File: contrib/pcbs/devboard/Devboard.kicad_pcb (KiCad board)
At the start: 2 copper layers, 42.5 x 36.8 mm, 11 parts, among them J1 Power, J2 Left, J3 ARM-JTAG, J4 Right, J5 JTAG, SW1 RESET, U1 TRADFRI

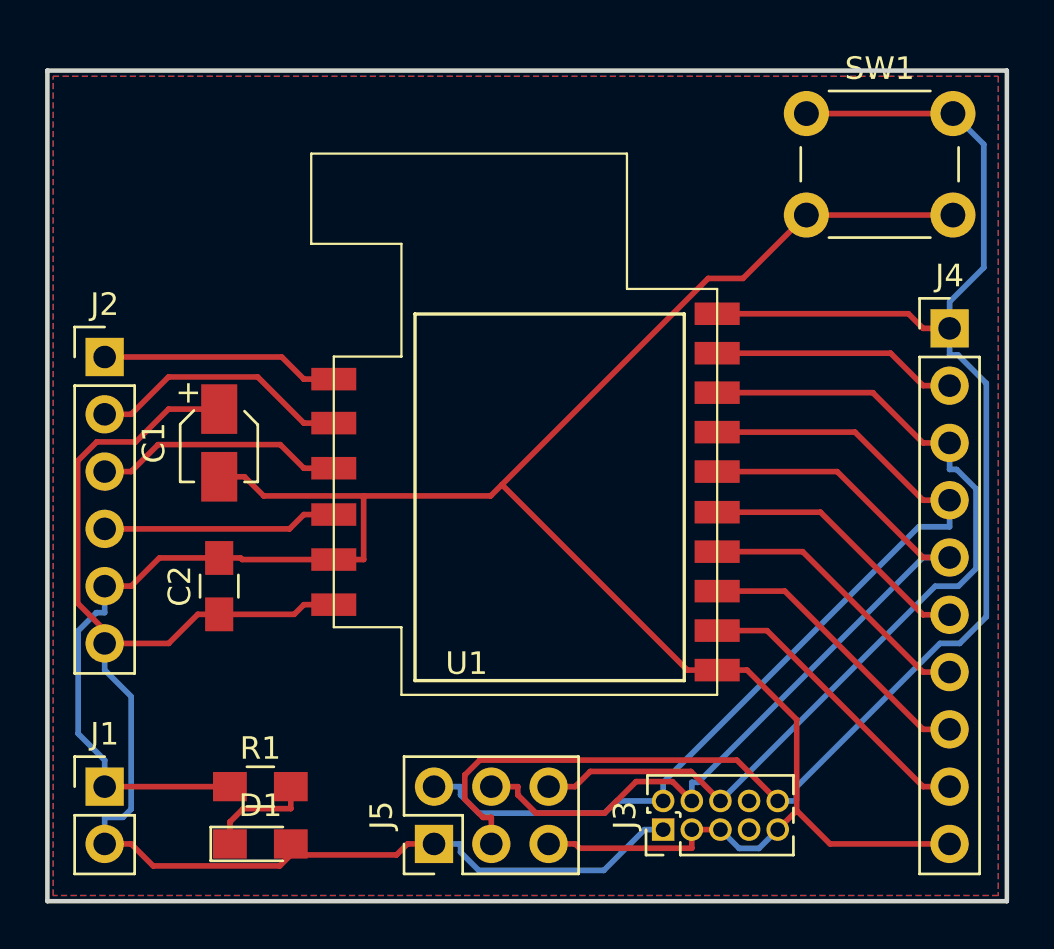
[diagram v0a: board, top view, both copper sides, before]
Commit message: Rework contributed PCBs
* Upgrade to KiCad 8
* Improved PCBs
* Added Makefile for automation of schema and board renders
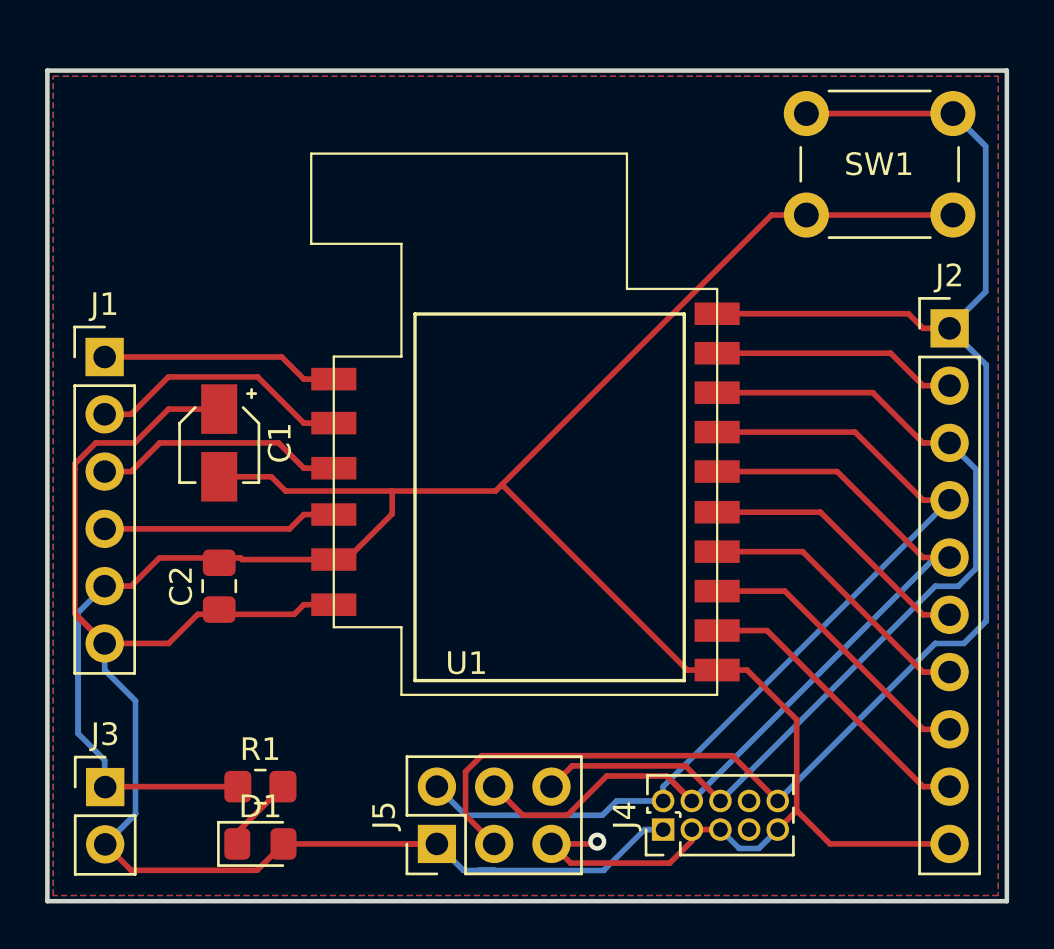
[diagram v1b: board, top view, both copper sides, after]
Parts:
- C1: value CP -> 10µF; footprint Capacitors_SMD:CP_Elec_3x5.3 -> Capacitor_SMD:CP_Elec_3x5.3
- C2: value C -> 100nF; footprint Capacitors_SMD:C_0805_HandSoldering -> Capacitor_SMD:C_0805_2012Metric_Pad1.18x1.45mm_HandSolder
- D1: footprint LEDs:LED_0805_HandSoldering -> LED_SMD:LED_0805_2012Metric_Pad1.15x1.40mm_HandSolder
- J1: value Power -> Left; footprint Pin_Headers:Pin_Header_Straight_1x02_Pitch2.54mm -> Connector_PinHeader_2.54mm:PinHeader_1x06_P2.54mm_Vertical
- J2: value Left -> Right; footprint Pin_Headers:Pin_Header_Straight_1x06_Pitch2.54mm -> Connector_PinHeader_2.54mm:PinHeader_1x10_P2.54mm_Vertical
- J3: value ARM-JTAG -> Power; footprint Pin_Headers:Pin_Header_Straight_2x05_Pitch1.27mm -> Connector_PinHeader_2.54mm:PinHeader_1x02_P2.54mm_Vertical
- J4: value Right -> ARM-JTAG; footprint Pin_Headers:Pin_Header_Straight_1x10_Pitch2.54mm -> Connector_PinHeader_1.27mm:PinHeader_2x05_P1.27mm_Vertical
- J5: footprint Pin_Headers:Pin_Header_Straight_2x03_Pitch2.54mm -> Connector_PinHeader_2.54mm:PinHeader_2x03_P2.54mm_Vertical
- R1: footprint Resistors_SMD:R_0805_HandSoldering -> Resistor_SMD:R_0805_2012Metric_Pad1.20x1.40mm_HandSolder
- SW1: value RESET -> Reset; footprint Buttons_Switches_THT:SW_PUSH_6mm -> Button_Switch_THT:SW_PUSH_6mm
- moved J2 37.5 mm to (181.0, 104.1)
- moved J4 25.6 mm to (168.3, 126.4), turned to 90 degrees
- moved J3 24.8 mm to (143.5, 124.5), turned to 0 degrees
- moved J1 19.0 mm to (143.5, 105.4)
- moved J5 0.13 mm to (158.2, 127.0)
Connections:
- J1 pad 1: GND -> Net-(J1-Pin_1)
- J1 pad 2: +3V3 -> Net-(J1-Pin_2)
- J2 pad 1: Net-(J2-Pad1) -> /RESETn
- J2 pad 2: Net-(J2-Pad2) -> Net-(J2-Pin_2)
- J2 pad 3: Net-(J2-Pad3) -> /SWO
- J2 pad 4: Net-(J2-Pad4) -> /SWDIO
- J2 pad 5: GND -> /SWCLK
- J2 pad 6: +3V3 -> Net-(J2-Pin_6)
- J3 pad 1: +3V3 -> GND
- J3 pad 2: /SWDIO -> +3V3
- J4 pad 1: /RESETn -> +3V3
- J4 pad 10: GND -> /RESETn
- J4 pad 2: Net-(J4-Pad2) -> /SWDIO
- J4 pad 3: /SWO -> GND
- J4 pad 4: /SWDIO -> /SWCLK
- J4 pad 5: /SWCLK -> GND
- J4 pad 6: Net-(J4-Pad6) -> /SWO
- J4 pad 7: Net-(J4-Pad7) -> unconnected-(J4-Pin_7-Pad7)
- J4 pad 8: Net-(J4-Pad8) -> unconnected-(J4-Pin_8-Pad8)
- J4 pad 9: Net-(J4-Pad9) -> GND
- U1 pad 1: Net-(J2-Pad1) -> Net-(J1-Pin_1)
- U1 pad 10: Net-(J4-Pad7) -> Net-(J2-Pin_7)
- U1 pad 11: Net-(J4-Pad6) -> Net-(J2-Pin_6)
- U1 pad 15: Net-(J4-Pad2) -> Net-(J2-Pin_2)
- U1 pad 2: Net-(J2-Pad2) -> Net-(J1-Pin_2)
- U1 pad 3: Net-(J2-Pad3) -> Net-(J1-Pin_3)
- U1 pad 4: Net-(J2-Pad4) -> Net-(J1-Pin_4)
- U1 pad 8: Net-(J4-Pad9) -> Net-(J2-Pin_9)
- U1 pad 9: Net-(J4-Pad8) -> Net-(J2-Pin_8)
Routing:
- net Net-(J4-Pad9): track 13.2 -> 0.00 mm
- net Net-(J2-Pin_9): track 0.00 -> 13.2 mm
- net Net-(J4-Pad8): track 12.8 -> 0.00 mm
- net Net-(J2-Pin_8): track 0.00 -> 12.8 mm
- net Net-(J4-Pad7): track 12.5 -> 0.00 mm
- net Net-(J2-Pin_7): track 0.00 -> 12.5 mm
- net Net-(J4-Pad6): track 12.2 -> 0.00 mm
- net Net-(J2-Pin_6): track 0.00 -> 12.2 mm
- net Net-(J2-Pad2): track 11.7 -> 0.00 mm
- net Net-(J1-Pin_2): track 0.00 -> 11.7 mm
- net Net-(J1-Pin_3): track 0.00 -> 11.2 mm
- net Net-(J2-Pad3): track 11.1 -> 0.00 mm
- net Net-(J4-Pad2): track 10.9 -> 0.00 mm
- net Net-(J2-Pin_2): track 0.00 -> 10.9 mm
- net Net-(J2-Pad1): track 10.6 -> 0.00 mm
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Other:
- net class Default removed
- rule pad_to_mask_clearance: 0.2 -> 0
